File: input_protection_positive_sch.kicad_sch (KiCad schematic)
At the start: 28 parts, among them Q1 SQM120P06, Q2 SQM120P06, U1 ADM1270

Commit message: Removed unused thermal jumpers. Added more thermal vias to Q1 and Q2. Realigned pitch numbers to a 5.08 mm grid
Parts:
- removed JP2: Thermal, Resistor_SMD:R_0612_1632Metric, symbol Jumper:Jumper_2_Bridged
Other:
- note added: "Thermal image taken (24 °C ambient): - 15V @ 16 A (1503) - 15V @ 14 A (1512) - 15V @ 12 A (1522)"
- note added: "Thermal image taken (24 °C ambient, THJ): - 15V @ 12 A (1544) - 15V @ 14 A (1555) - 15V @ 16 A (1604)"
- note removed: "Thermal image taken: - 24V @ 12 A - 18V @ 14 A - 20V @ 16 A"
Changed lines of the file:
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@@
   (junction (at 259.08 64.77) (diameter 0) (color 0 0 0 0)
-  )
-  (junction (at 209.55 64.77) (diameter 0) (color 0 0 0 0)
   )
   (junction (at 173.99 64.77) (diameter 0) (color 0 0 0 0)
@@
     (stroke (width 0) (type default))
   )
-  (wire (pts (xy 209.55 62.23) (xy 209.55 64.77))
-    (stroke (width 0) (type default))
-  )
   (wire (pts (xy 58.42 64.77) (xy 64.77 64.77))
     (stroke (width 0) (type default))
@@
     (stroke (width 0) (type default))
   )
-  (wire (pts (xy 214.63 48.26) (xy 209.55 48.26))
-    (stroke (width 0) (type default))
-  )
   (wire (pts (xy 45.72 64.77) (xy 45.72 67.31))
     (stroke (width 0) (type default))
@@
     (stroke (width 0) (type default))
   )
-  (wire (pts (xy 209.55 64.77) (xy 228.6 64.77))
-    (stroke (width 0) (type default))
-  )
   (wire (pts (xy 173.99 73.66) (xy 173.99 80.01))
     (stroke (width 0) (type default))
@@
     (stroke (width 0) (type default))
   )
-  (wire (pts (xy 209.55 48.26) (xy 209.55 52.07))
-    (stroke (width 0) (type default))
-  )
   (wire (pts (xy 166.37 78.74) (xy 154.94 78.74))
     (stroke (width 0) (type default))
@@
     (stroke (width 0) (type default))
   )
-  (wire (pts (xy 189.23 64.77) (xy 209.55 64.77))
+  (wire (pts (xy 189.23 64.77) (xy 228.6 64.77))
     (stroke (width 0) (type default))
   )
   (wire (pts (xy 175.26 110.49) (xy 175.26 111.76))
-    (stroke (width 0) (type default))
-  )
-  (wire (pts (xy 214.63 49.53) (xy 214.63 48.26))
     (stroke (width 0) (type default))
   )
@@
     (effects (font (size 1.27 1.27)) (justify left bottom))
   )
-  (text "Thermal image taken:\n- 24V @ 12 A\n- 18V @ 14 A\n- 20V @ 16 A"
+  (text "Thermal image taken (24 °C ambient):\n- 15V @ 16 A (1503)\n- 15V @ 14 A (1512)\n- 15V @ 12 A (1522)\n"
     (at 24.13 180.34 0)
     (effects (font (size 1.27 1.27)) (justify left bottom))
@@
   (text "Maximum FET power: 70 W (the positive side uses about the same. See ADM1270 Excel sheet)\nRPWR = 1.42e5 * RS * PFET(LIM) = 1.42e5 * 3e-3 * 70 = 30k"
     (at 156.21 41.91 0)
+    (effects (font (size 1.27 1.27)) (justify left bottom))
+  )
+  (text "Thermal image taken (24 °C ambient, THJ):\n- 15V @ 12 A (1544)\n- 15V @ 14 A (1555)\n- 15V @ 16 A (1604)\n"
+    (at 22.86 190.5 0)
     (effects (font (size 1.27 1.27)) (justify left bottom))
   )
@@
         )
       )
-    )
-  )
-  (symbol (lib_id "Jumper:Jumper_2_Bridged") (at 209.55 57.15 90) (unit 1)
-    (in_bom yes) (on_board yes) (dnp no) (fields_autoplaced)
-    (property "Reference" "JP2" (at 210.82 55.88 90)
-      (effects (font (size 1.27 1.27)) (justify right))
-    )
-    (property "Value" "Thermal" (at 210.82 58.42 90)
-      (effects (font (size 1.27 1.27)) (justify right))
-    )
-    (property "Footprint" "Resistor_SMD:R_0612_1632Metric" (at 209.55 57.15 0)
-      (effects (font (size 1.27 1.27)) hide)
-    )
-    (property "Datasheet" "~" (at 209.55 57.15 0)
-      (effects (font (size 1.27 1.27)) hide)
-    )
-    (property "MFN" "Vishay" (at 209.55 57.15 0)
-      (effects (font (size 1.27 1.27)) hide)
-    )
-    (property "PN" "THJP0612AST1" (at 209.55 57.15 0)
-      (effects (font (size 1.27 1.27)) hide)
-    )
-    (property "RoHS" "Yes" (at 209.55 57.15 0)
-      (effects (font (size 1.27 1.27)) hide)
-    )
-    (property "Temperature" "Tstorage = –65 °C to 150 °C" (at 209.55 57.15 0)
-      (effects (font (size 1.27 1.27)) hide)
-    )
-    (pin "2")
-    (pin "1")
-    (instances
-      (project "backplane"
-        (path "/b4ace06a-3ad4-479e-aaa4-d547ecf6903f/f9160387-088e-4a7b-8d58-b2647e07444c"
-          (reference "JP2") (unit 1)
-        )
-      )
-    )
-  )
-  (symbol (lib_id "power:Earth") (at 214.63 49.53 0) (unit 1)
-    (in_bom yes) (on_board yes) (dnp no) (fields_autoplaced)
-    (property "Reference" "#PWR071" (at 214.63 55.88 0)
-      (effects (font (size 1.27 1.27)) hide)
-    )
-    (property "Value" "Earth" (at 214.63 53.34 0)
-      (effects (font (size 1.27 1.27)) hide)
-    )
-    (property "Footprint" "" (at 214.63 49.53 0)
-      (effects (font (size 1.27 1.27)) hide)
-    )
-    (property "Datasheet" "~" (at 214.63 49.53 0)
-      (effects (font (size 1.27 1.27)) hide)
-    )
-    (pin "1")
-    (instances
-      (project "backplane"
-        (path "/b4ace06a-3ad4-479e-aaa4-d547ecf6903f/f9160387-088e-4a7b-8d58-b2647e07444c"
-          (reference "#PWR071") (unit 1)
-        )
-      )

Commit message: Updated libraries Removed thermal jumpers apart from one, because they are not needed
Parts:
- removed JP3: Thermal, Resistor_SMD:R_0612_1632Metric, symbol Jumper:Jumper_2_Bridged
- JP1: now not fitted
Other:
- note added: "The thermal jumper is not required. Test to see if it makes a difference"
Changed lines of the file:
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@@
   (junction (at 163.83 97.79) (diameter 0) (color 0 0 0 0)
-  )
-  (junction (at 64.77 64.77) (diameter 0) (color 0 0 0 0)
   )
   (junction (at 116.84 64.77) (diameter 0) (color 0 0 0 0)
@@
     (stroke (width 0) (type default))
   )
-  (wire (pts (xy 64.77 62.23) (xy 64.77 64.77))
-    (stroke (width 0) (type default))
-  )
   (wire (pts (xy 27.94 73.66) (xy 27.94 74.93))
     (stroke (width 0) (type default))
@@
     (stroke (width 0) (type default))
   )
-  (wire (pts (xy 58.42 64.77) (xy 64.77 64.77))
-    (stroke (width 0) (type default))
-  )
   (wire (pts (xy 116.84 64.77) (xy 147.32 64.77))
     (stroke (width 0) (type default))
@@
     (stroke (width 0) (type default))
   )
-  (wire (pts (xy 69.85 49.53) (xy 69.85 48.26))
-    (stroke (width 0) (type default))
-  )
   (wire (pts (xy 228.6 86.36) (xy 228.6 87.63))
     (stroke (width 0) (type default))
@@
     (stroke (width 0) (type default))
   )
-  (wire (pts (xy 64.77 48.26) (xy 64.77 52.07))
-    (stroke (width 0) (type default))
-  )
   (wire (pts (xy 142.24 106.68) (xy 142.24 107.95))
     (stroke (width 0) (type default))
@@
     (stroke (width 0) (type default))
   )
-  (wire (pts (xy 69.85 48.26) (xy 64.77 48.26))
-    (stroke (width 0) (type default))
-  )
-  (wire (pts (xy 64.77 64.77) (xy 76.2 64.77))
+  (wire (pts (xy 58.42 64.77) (xy 76.2 64.77))
     (stroke (width 0) (type default))
   )
@@
   (text "Q1:\nMeasured Temp @ 12A: 63.6 °C (on tab)\nMeasured Temp @ 14A: 80.3 °C (on tab)\nMeasured Temp @ 15A: 86.7 °C (on tab)\nMeasured Temp @ 16A: 98.5 °C (on tab)\nAmbient: 24.4 °C"
     (at 46.99 146.05 0)
+    (effects (font (size 1.27 1.27)) (justify left bottom))
+  )
+  (text "The thermal jumper is not required.\nTest to see if it makes a difference"
+    (at 115.57 45.72 0)
     (effects (font (size 1.27 1.27)) (justify left bottom))
   )
@@
     )
   )
-  (symbol (lib_id "power:Earth") (at 69.85 49.53 0) (unit 1)
-    (in_bom yes) (on_board yes) (dnp no) (fields_autoplaced)
-    (property "Reference" "#PWR069" (at 69.85 55.88 0)
-      (effects (font (size 1.27 1.27)) hide)
-    )
-    (property "Value" "Earth" (at 69.85 53.34 0)
-      (effects (font (size 1.27 1.27)) hide)
-    )
-    (property "Footprint" "" (at 69.85 49.53 0)
-      (effects (font (size 1.27 1.27)) hide)
-    )
-    (property "Datasheet" "~" (at 69.85 49.53 0)
-      (effects (font (size 1.27 1.27)) hide)
-    )
-    (pin "1")
-    (instances
-      (project "backplane"
-        (path "/b4ace06a-3ad4-479e-aaa4-d547ecf6903f/f9160387-088e-4a7b-8d58-b2647e07444c"
-          (reference "#PWR069") (unit 1)
-        )
-      )
-    )
-  )
   (symbol (lib_id "Device:Q_PMOS_GDS") (at 93.98 67.31 90) (unit 1)
     (in_bom yes) (on_board yes) (dnp no) (fields_autoplaced)
@@
         (path "/b4ace06a-3ad4-479e-aaa4-d547ecf6903f/f9160387-088e-4a7b-8d58-b2647e07444c"
           (reference "NT2") (unit 1)
-        )
-      )
-    )
-  )
-  (symbol (lib_id "Jumper:Jumper_2_Bridged") (at 64.77 57.15 90) (unit 1)
-    (in_bom yes) (on_board yes) (dnp no) (fields_autoplaced)
-    (property "Reference" "JP3" (at 66.04 55.88 90)
-      (effects (font (size 1.27 1.27)) (justify right))
-    )
-    (property "Value" "Thermal" (at 66.04 58.42 90)
-      (effects (font (size 1.27 1.27)) (justify right))
-    )
-    (property "Footprint" "Resistor_SMD:R_0612_1632Metric" (at 64.77 57.15 0)
-      (effects (font (size 1.27 1.27)) hide)
-    )
-    (property "Datasheet" "~" (at 64.77 57.15 0)
-      (effects (font (size 1.27 1.27)) hide)
-    )
-    (property "MFN" "Vishay" (at 64.77 57.15 0)
-      (effects (font (size 1.27 1.27)) hide)
-    )
-    (property "PN" "THJP0612AST1" (at 64.77 57.15 0)
-      (effects (font (size 1.27 1.27)) hide)
-    )
-    (property "RoHS" "Yes" (at 64.77 57.15 0)
-      (effects (font (size 1.27 1.27)) hide)
-    )
-    (property "Temperature" "Tstorage = –65 °C to 150 °C" (at 64.77 57.15 0)
-      (effects (font (size 1.27 1.27)) hide)
-    )
-    (pin "2")
-    (pin "1")
-    (instances
-      (project "backplane"
-        (path "/b4ace06a-3ad4-479e-aaa4-d547ecf6903f/f9160387-088e-4a7b-8d58-b2647e07444c"
-          (reference "JP3") (unit 1)
         )
       )
@@
   )
   (symbol (lib_id "Jumper:Jumper_2_Bridged") (at 147.32 57.15 90) (unit 1)
-    (in_bom yes) (on_board yes) (dnp no) (fields_autoplaced)
+    (in_bom yes) (on_board yes) (dnp yes) (fields_autoplaced)
     (property "Reference" "JP1" (at 148.59 55.88 90)
       (effects (font (size 1.27 1.27)) (justify right))

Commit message: Updated libraries Added DNP property for KiCost
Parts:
- TP1: DNP (none) -> 1
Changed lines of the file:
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@@
+      (effects (font (size 1.27 1.27)) hide)
+    )
+    (property "DNP" "1" (at 76.2 63.5 0)
       (effects (font (size 1.27 1.27)) hide)
     )

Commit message: Replaced constant current diode with KiCad device available as of v7.0.10 Updated LM5067 3D model
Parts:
- renumbered C22 to C1, C22 to C15, D1 to D2, R2 to R1, R2 to R10

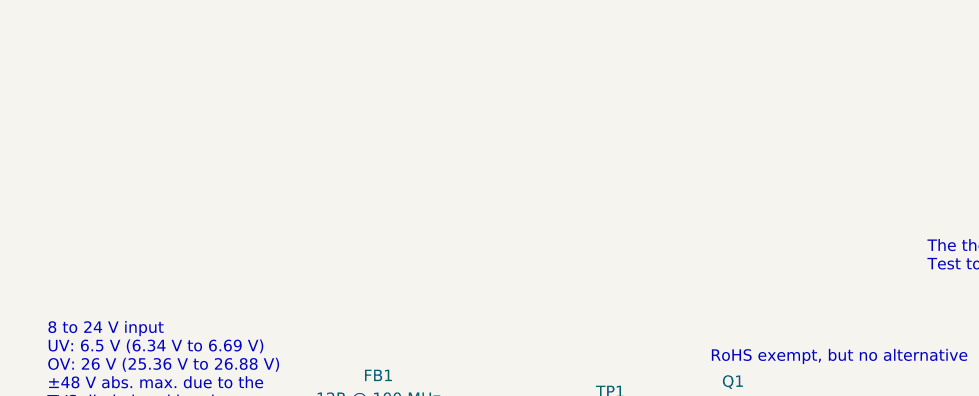
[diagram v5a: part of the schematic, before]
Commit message: Added info about thermals
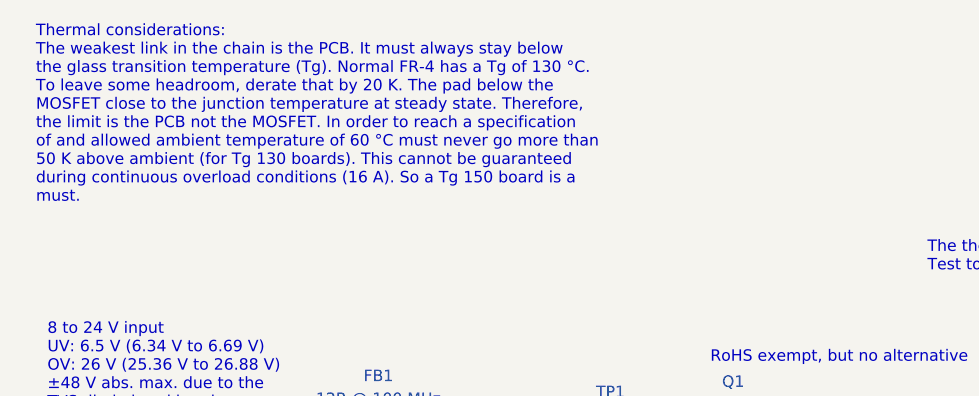
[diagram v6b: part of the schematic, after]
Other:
- note added: "Thermal considerations: The weakest link in the chain is the PCB. It must always stay below the glass transition temperature (Tg). Normal FR-4 has a Tg of 130 °C. To leave some headroom, derate that by 20 K. The pad below the MOSFET close to the junction temperature at steady state. Therefore, the limit is the PCB not the MOSFET. In order to reach a specification of and allowed ambient temperatur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"
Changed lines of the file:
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@@
+    (effects (font (size 1.27 1.27)) (justify left bottom))
+  )
+  (text "Thermal considerations:\nThe weakest link in the chain is the PCB. It must always stay below\nthe glass transition temperature (Tg). Normal FR-4 has a Tg of 130 °C.\nTo leave some headroom, derate that by 20 K. The pad below the\nMOSFET close to the junction temperature at steady state. Therefore,\nthe limit is the PCB not the MOSFET. In order to reach a specification\nof and allowed ambient temperature of 60 °C must never go more than\n50 K above ambient (for Tg 130 boards). This cannot be guaranteed\nduring continuous overload conditions (16 A). So a Tg 150 board is a\nmust."
+    (at 16.51 38.1 0)
     (effects (font (size 1.27 1.27)) (justify left bottom))
   )

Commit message: Updated power MOSFET PNs to match Mouser
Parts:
- Q1, Q2: PN SQM120P06-07L -> SQM120P06-07L_GE3
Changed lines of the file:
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@@
       (effects (font (size 1.27 1.27)) hide)
     )
-    (property "PN" "SQM120P06-07L" (at 93.98 67.31 0)
+    (property "PN" "SQM120P06-07L_GE3" (at 93.98 67.31 0)
       (effects (font (size 1.27 1.27)) hide)
     )
@@
       (effects (font (size 1.27 1.27)) hide)
     )
-    (property "PN" "SQM120P06-07L" (at 184.15 67.31 0)
+    (property "PN" "SQM120P06-07L_GE3" (at 184.15 67.31 0)
       (effects (font (size 1.27 1.27)) hide)
     )
